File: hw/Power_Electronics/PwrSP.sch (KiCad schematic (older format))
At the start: 21 parts, among them J2 POWER_INPUT, J3 OUTPUT POWER, U2 AMS1117

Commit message: update schematic with hall and BEMF circuits
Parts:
- removed JP? (x2): Jumper_2_Open, symbol Jumper:Jumper_2_Open
- added C? (x6): 10pF, Capacitor_SMD:C_0603_1608Metric, symbol Device:C
- added D? (x9): B5819W, inversor-pmsm:D_SOD-123, symbol Device:D_Schottky
- added D? (x3): RS1J, Diode_SMD:D_SMA, symbol Device:D
- added JP? (x2): Jumper_2_Open, Jumper:SolderJumper-2_P1.3mm_Open_TrianglePad1.0x1.5mm, symbol Jumper:Jumper_2_Open
- added JP? (x3): Jumper_3_Open, Jumper:SolderJumper-3_P2.0mm_Open_TrianglePad1.0x1.5mm, symbol Jumper:Jumper_3_Open
- added R? (x3): 2K, Resistor_SMD:R_0603_1608Metric, symbol Device:R
- added R? (x3): 10K, Resistor_SMD:R_0603_1608Metric, symbol Device:R
- added R? (x3): DNM, Resistor_SMD:R_0603_1608Metric, symbol Device:R
- added R? (x6): 100K, Resistor_SMD:R_0805_2012Metric, symbol Device:R
- added R? (x3): 1K, Resistor_SMD:R_0603_1608Metric, symbol Device:R
- added R? (x3): 5.6K, Resistor_SMD:R_0805_2012Metric, symbol Device:R
- JP?: footprint (none) -> Jumper:SolderJumper-2_P1.3mm_Open_TrianglePad1.0x1.5mm
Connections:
- net +3V3: now also JP?.2 (B), D?.1 (K), D?.1 (K), D?.1 (K), D?.1 (K), D?.1 (K), D?.1 (K), R?.1, R?.1, R?.1
- net +5V: now also JP?.2 (B)
- net GND: now also C?.1, C?.1, C?.1, C?.1, C?.1, C?.1, R?.2, R?.2, R?.2
- net OUT1: now also R?.1, R?.2
- net OUT2: now also R?.1, R?.2
- net OUT3: now also R?.1, R?.2
- net at J?.1 (Pin_1): now also R?.2
- net at J?.2 (Pin_2): now also R?.2
- net at J?.3 (Pin_3): now also R?.2
- net at J?.4 (Pin_4), JP?.1 (A): now also JP?.1 (A), JP?.1 (A)
- new net: R?.1, R?.2 (x3)
- new net: D?.1 (K), R?.1 (x3)
- new net: D?.2 (A), R?.2 (x3)
- new net +12V: JP?.2 (B)
- new net BEMF_A: C?.2, D?.2 (A), D?.2 (A), JP?.3 (B), R?.1, R?.2
- new net BEMF_B: C?.2, D?.2 (A), D?.2 (A), JP?.3 (B), R?.1, R?.2
- new net BEMF_C: C?.2, D?.2 (A), D?.2 (A), JP?.3 (B), R?.1, R?.2
- new net ENC_HALL_A: C?.2, D?.2 (A), JP?.1 (A), R?.1, R?.1, R?.2
- new net ENC_HALL_B: C?.2, D?.2 (A), JP?.1 (A), R?.1, R?.1, R?.2
- new net ENC_HALL_C: C?.2, D?.2 (A), JP?.1 (A), R?.1, R?.1, R?.2
- new net GPIO_BEMF: D?.1 (K), D?.1 (K), D?.1 (K)
- new net HALL1: JP?.2 (C)
- new net HALL2: JP?.2 (C)
- new net HALL3: JP?.2 (C)
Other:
- note added: "A+/H1"
- note added: "B+/H2"
- note added: "GND"
- note added: "U"
- note added: "V"
- note added: "VDD"
- note added: "W"
- note added: "Z+/H3"
- moved on the sheet: J?, JP?

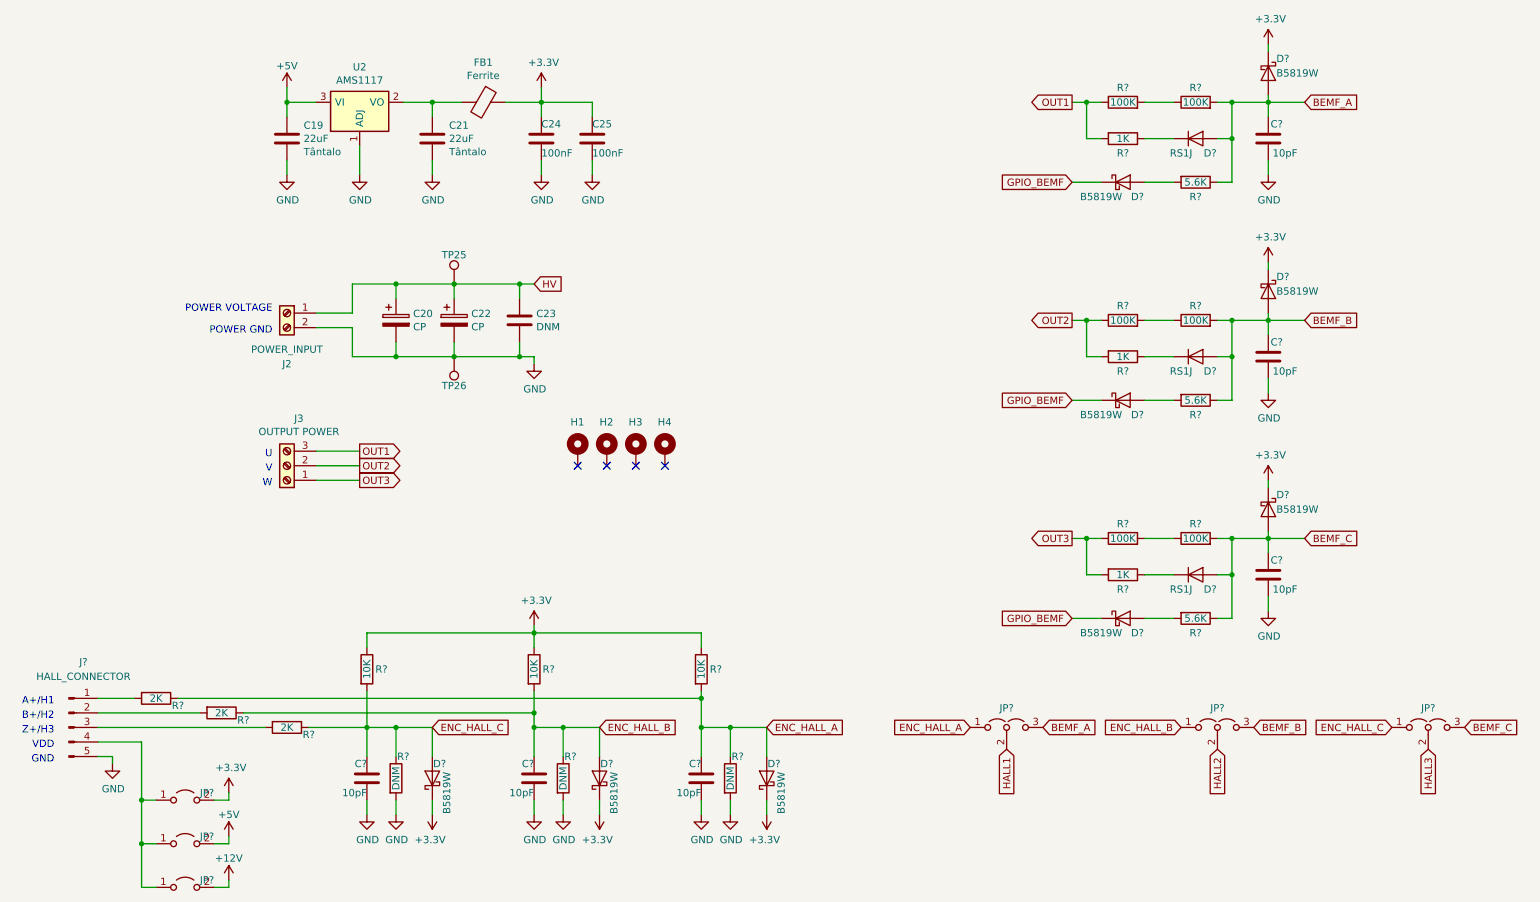
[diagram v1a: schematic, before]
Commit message: all component's positions are more or less defined
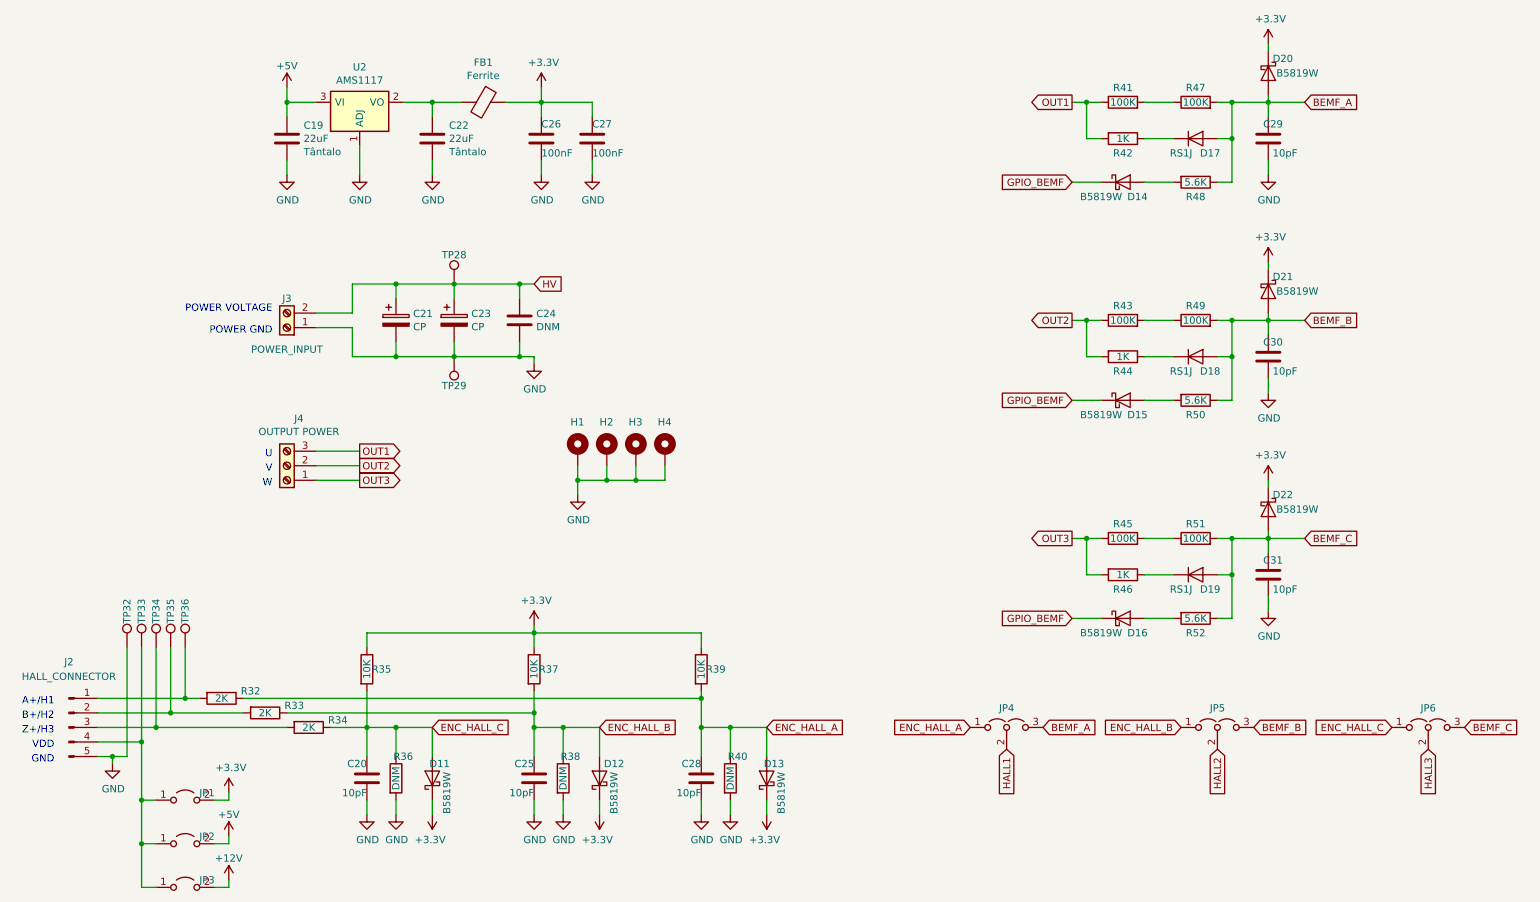
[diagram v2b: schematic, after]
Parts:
- added TP32, TP33, TP34, TP35, TP36: TestPoint, TestPoint:TestPoint_Pad_D1.5mm, symbol Connector:TestPoint
- C21: renamed from C20; footprint Capacitor_THT:CP_Radial_D18.0mm_P7.50mm -> inversor-pmsm:CP_Radial_D18.0mm_P7.50mm_universal
- C23: renamed from C22; footprint Capacitor_SMD:CP_Elec_10x10 -> (none)
- J2: renamed from J?; footprint (none) -> Connector_PinHeader_2.54mm:PinHeader_1x05_P2.54mm_Vertical
- JP4, JP5, JP6: renamed from JP?; footprint Jumper:SolderJumper-3_P2.0mm_Open_TrianglePad1.0x1.5mm -> inversor-pmsm:SolderJumper-3_P2.0mm_Open_TrianglePad1.0x1.5mm_custom
- gave numbers to parts that had none: 42
- renumbered C21 to C22, C23 to C24, C24 to C26, C25 to C27, J2 to J3, J3 to J4, TP25 to TP28, TP26 to TP29
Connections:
- net GND: now also H1.1, H2.1, H3.1, H4.1, J3.1 (Pin_1), TP32.1; no longer J3.2 (Pin_2)
- net HV: now also J3.2 (Pin_2); no longer J3.1 (Pin_1)
- net at J2.3 (Pin_3), R34.2: now also TP34.1
- net at J2.2 (Pin_2), R33.2: now also TP35.1
- net at J2.1 (Pin_1), R32.2: now also TP36.1
- net at J2.4 (Pin_4), JP1.1 (A), JP2.1 (A)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: now also TP33.1
- no-connect marks 4 -> 0
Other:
- moved on the sheet: R32, R33, R34

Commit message: adjustments made on silkscreen layer
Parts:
- removed C24: DNM, Capacitor_SMD:C_0805_2012Metric, symbol Device:C
- added H1, H2, H3, H4, H5: MountingHole_Pad, inversor-pmsm:MountingHole_3.4mm_M3_Pad_Via, symbol Mechanical:MountingHole_Pad
- added H10, H11, H12, H13, H14: MountingHole_Pad, MountingHole:MountingHole_2.2mm_M2_DIN965_Pad, symbol Mechanical:MountingHole_Pad
- added J6: POWER_INPUT, inversor-pmsm:Amass_XT60PW-M_Kombifootprint, symbol Connector:Screw_Terminal_01x02
- added JP4: Jumper, Jumper:SolderJumper-2_P1.3mm_Open_TrianglePad1.0x1.5mm, symbol Device:Jumper
- added TP34, TP35, TP38, TP39: TestPoint, TestPoint:TestPoint_Pad_D1.5mm, symbol Connector:TestPoint
- C27: renamed from C23; footprint (none) -> inversor-pmsm:CP_Radial_D18.0mm_P7.50mm_universal
- D17, D18, D19: footprint Diode_SMD:D_SMA -> inversor-pmsm:D_SMA_custom
- J4: renamed from J3; footprint TerminalBlock:TerminalBlock_bornier-2_P5.08mm -> (none)
- J5: renamed from J4; footprint TerminalBlock:TerminalBlock_bornier-3_P5.08mm -> (none)
- renumbered C19 to C23, C20 to C24, C21 to C25, C22 to C26, C25 to C28, C26 to C29, C27 to C30, C28 to C31, C29 to C32, C30 to C33, C31 to C34, H1 to H6, H2 to H7, H3 to H8, H4 to H9, J2 to J3, JP4 to JP5, JP5 to JP6, JP6 to JP7, R32 to R40, R33 to R41, R34 to R42, R35 to R43, R36 to R44, R37 to R45, R38 to R46, R39 to R47, R40 to R48, R41 to R49, R42 to R50, R43 to R51, R44 to R52, R45 to R53, R46 to R54, R47 to R55, R48 to R56, R49 to R57, R50 to R58, R51 to R59, R52 to R60, TP32 to TP29, TP33 to TP30, TP34 to TP31, TP35 to TP32, TP36 to TP33, TP28 to TP36, TP29 to TP37
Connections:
- net +3V3: now also TP39.1
- net +5V: now also TP34.1
- net GND: now also H10.1, H3.1, J6.1 (Pin_1), JP4.2, TP35.1, TP38.1
- net GPIO_BEMF: now also JP4.1
- net HV: now also H1.1, H12.1, J6.2 (Pin_2)
- net OUT1: now also H11.1, H2.1
- net OUT2: now also H13.1, H4.1
- net OUT3: now also H14.1, H5.1
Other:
- moved on the sheet: C25, C27, J5, TP36, TP37

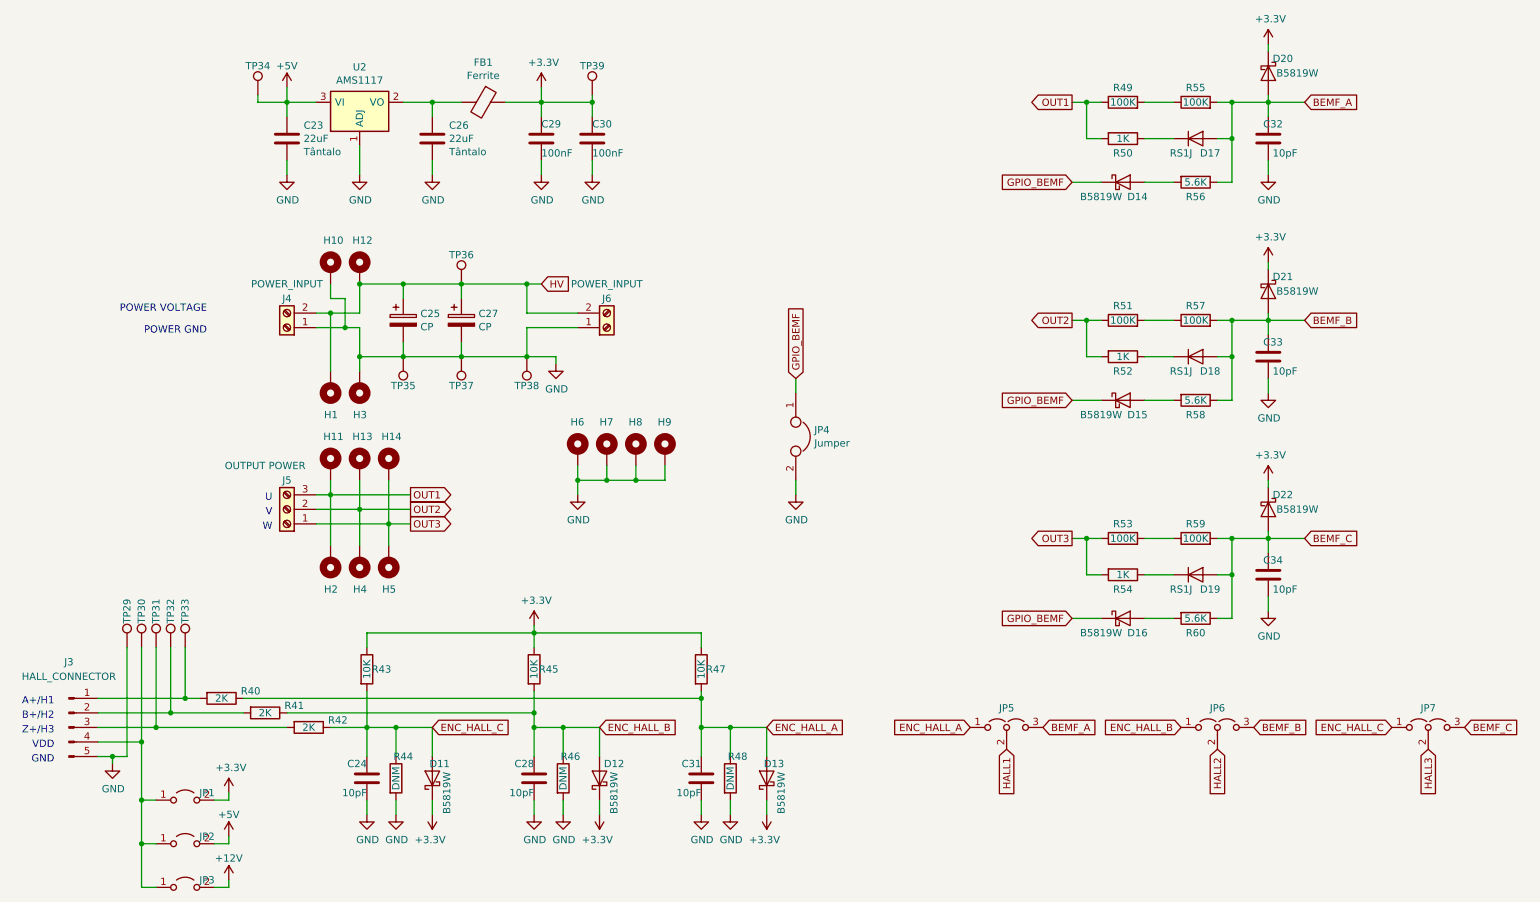
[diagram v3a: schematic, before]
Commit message: create high voltage net class and solve DRC erros
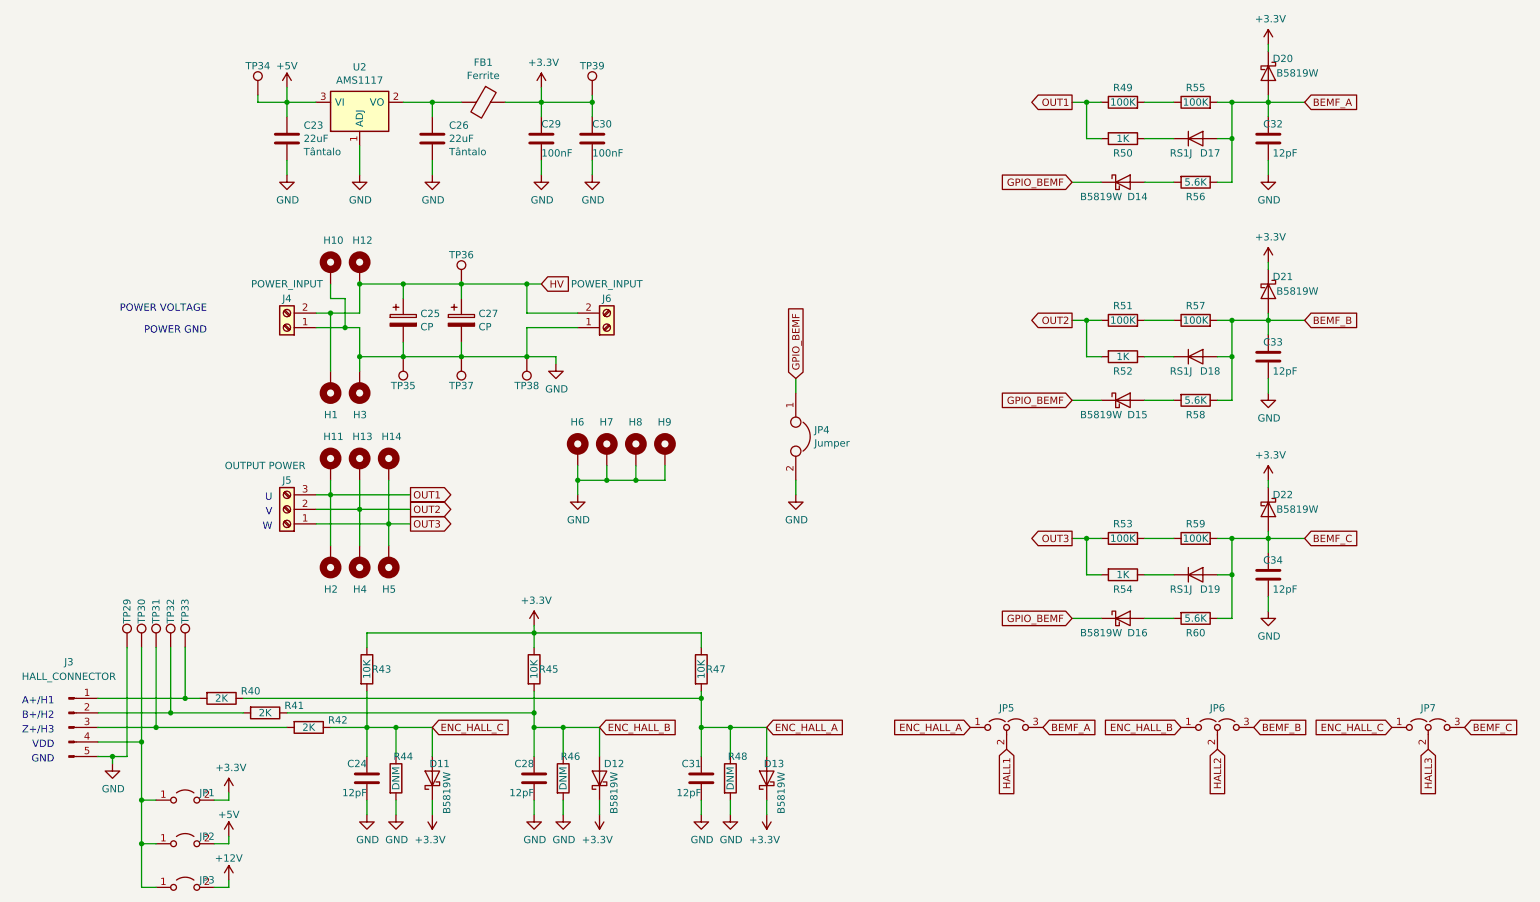
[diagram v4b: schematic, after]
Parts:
- C24, C28, C31, C32, C33, C34: value 10pF -> 12pF; LCSC C1634 -> C38523
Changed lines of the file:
@@
 AR Path="/6028AEA0/5FCBD726" Ref="C24"  Part="1"
 F 0 "C24" H 3050 6050 50  0000 L CNN
-F 1 "10pF" H 3050 6250 50  0000 L CNN
+F 1 "12pF" H 3050 6250 50  0000 L CNN
 F 2 "Capacitor_SMD:C_0603_1608Metric" H 3088 6000 50  0001 C CNN
 F 3 "Samsung-Electro-Mechanics-CL10C330JB8NNNC_C1663.pdf" H 3050 6150 50  0001 C CNN
-F 4 "C1634" H 3050 6150 50  0001 C CNN "LCSC"
+F 4 "C38523" H 3050 6150 50  0001 C CNN "LCSC"
 	1    3050 6150
 	-1   0    0    1
@@
 AR Path="/6028AEA0/5FD23B37" Ref="C28"  Part="1"
 F 0 "C28" H 4200 6050 50  0000 L CNN
-F 1 "10pF" H 4200 6250 50  0000 L CNN
+F 1 "12pF" H 4200 6250 50  0000 L CNN
 F 2 "Capacitor_SMD:C_0603_1608Metric" H 4238 6000 50  0001 C CNN
 F 3 "Samsung-Electro-Mechanics-CL10C330JB8NNNC_C1663.pdf" H 4200 6150 50  0001 C CNN
-F 4 "C1634" H 4200 6150 50  0001 C CNN "LCSC"
+F 4 "C38523" H 4200 6150 50  0001 C CNN "LCSC"
 	1    4200 6150
 	-1   0    0    1
@@
 AR Path="/6028AEA0/5FD29B02" Ref="C31"  Part="1"
 F 0 "C31" H 5350 6050 50  0000 L CNN
-F 1 "10pF" H 5350 6250 50  0000 L CNN
+F 1 "12pF" H 5350 6250 50  0000 L CNN
 F 2 "Capacitor_SMD:C_0603_1608Metric" H 5388 6000 50  0001 C CNN
 F 3 "Samsung-Electro-Mechanics-CL10C330JB8NNNC_C1663.pdf" H 5350 6150 50  0001 C CNN
-F 4 "C1634" H 5350 6150 50  0001 C CNN "LCSC"
+F 4 "C38523" H 5350 6150 50  0001 C CNN "LCSC"
 	1    5350 6150
 	-1   0    0    1
@@
 AR Path="/6028AEA0/5FE75328" Ref="C32"  Part="1"
 F 0 "C32" H 9150 1650 50  0000 L CNN
-F 1 "10pF" H 9050 1850 50  0000 L CNN
+F 1 "12pF" H 9050 1850 50  0000 L CNN
 F 2 "Capacitor_SMD:C_0603_1608Metric" H 9288 1600 50  0001 C CNN
 F 3 "Samsung-Electro-Mechanics-CL10C330JB8NNNC_C1663.pdf" H 9250 1750 50  0001 C CNN
-F 4 "C1634" H 9250 1750 50  0001 C CNN "LCSC"
+F 4 "C38523" H 9250 1750 50  0001 C CNN "LCSC"
 	1    9250 1750
 	-1   0    0    1
@@
 AR Path="/6028AEA0/5FEB7E08" Ref="C33"  Part="1"
 F 0 "C33" H 9150 3150 50  0000 L CNN
-F 1 "10pF" H 9050 3350 50  0000 L CNN
+F 1 "12pF" H 9050 3350 50  0000 L CNN
 F 2 "Capacitor_SMD:C_0603_1608Metric" H 9288 3100 50  0001 C CNN
 F 3 "Samsung-Electro-Mechanics-CL10C330JB8NNNC_C1663.pdf" H 9250 3250 50  0001 C CNN
-F 4 "C1634" H 9250 3250 50  0001 C CNN "LCSC"
+F 4 "C38523" H 9250 3250 50  0001 C CNN "LCSC"
 	1    9250 3250
 	-1   0    0    1
@@
 AR Path="/6028AEA0/5FEC0305" Ref="C34"  Part="1"
 F 0 "C34" H 9150 4650 50  0000 L CNN
-F 1 "10pF" H 9050 4850 50  0000 L CNN
+F 1 "12pF" H 9050 4850 50  0000 L CNN
 F 2 "Capacitor_SMD:C_0603_1608Metric" H 9288 4600 50  0001 C CNN
 F 3 "Samsung-Electro-Mechanics-CL10C330JB8NNNC_C1663.pdf" H 9250 4750 50  0001 C CNN
-F 4 "C1634" H 9250 4750 50  0001 C CNN "LCSC"
+F 4 "C38523" H 9250 4750 50  0001 C CNN "LCSC"
 	1    9250 4750
 	-1   0    0    1
